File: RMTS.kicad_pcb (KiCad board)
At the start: 2 copper layers, 78.1 x 50.2 mm, 86 parts, among them J1 Screw_Terminal_01x02, J10 CONN_02, J11 CONN_02, J12 CONN_02, J2 Programmer, J3 Screw_Terminal_01x03, J4 Screw_Terminal_01x04, J5 Screw_Terminal_01x02, J6 Screw_Terminal_01x02, J7 Micro_SD_Card_Det_Hirose_DM3AT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

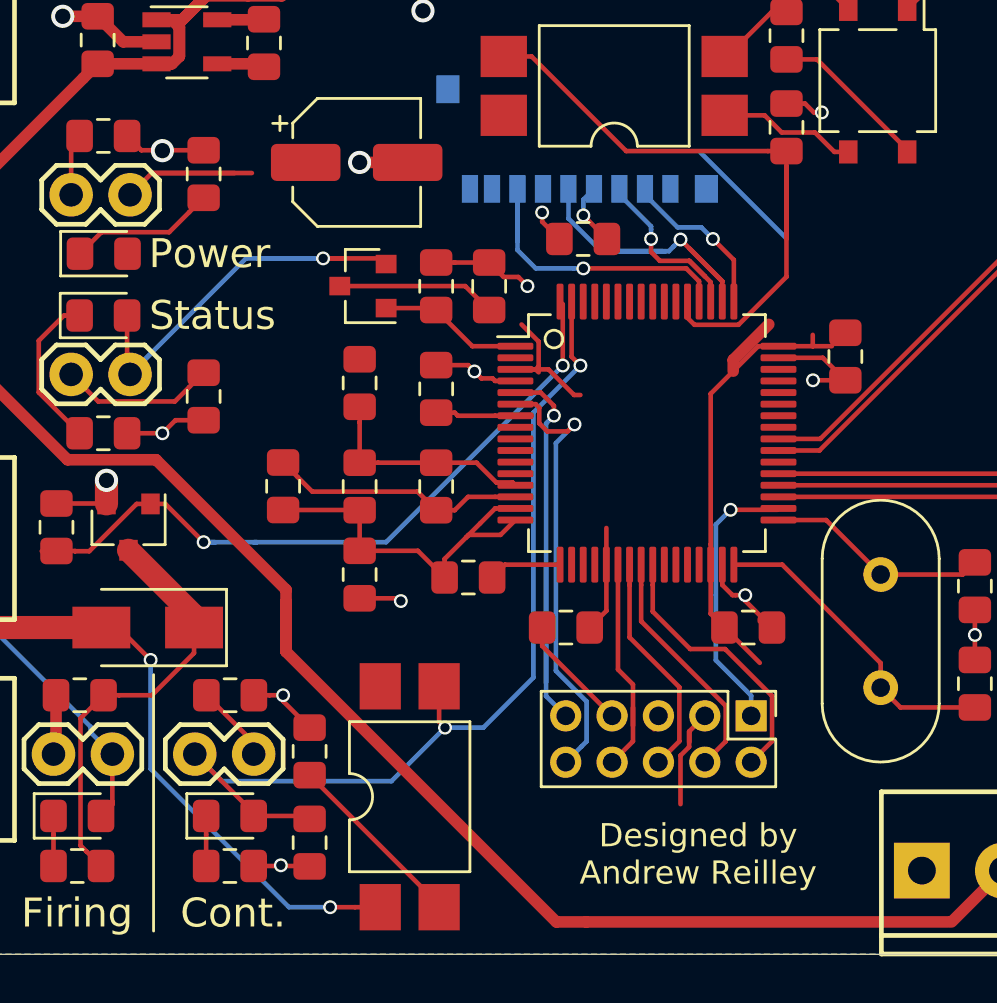
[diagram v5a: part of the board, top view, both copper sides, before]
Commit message: Adjust silkscreen
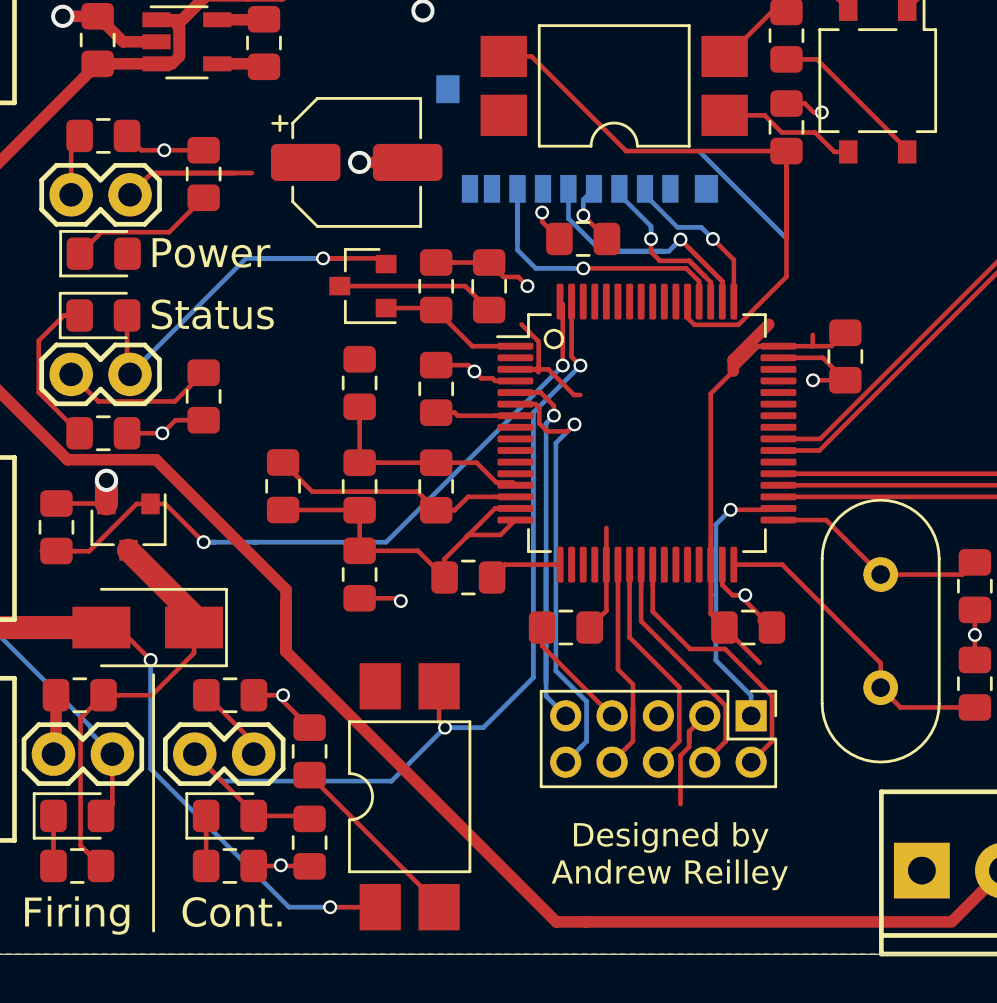
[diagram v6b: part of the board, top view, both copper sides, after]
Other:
- board text added: "Load Cell"
- board text added: "Main"
- board text added: "Pressure"
- board text added: "Pyro"
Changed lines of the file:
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@@
   (general
     (thickness 1.6)
-    (drawings 33)
-    (tracks 656)
+    (drawings 39)
+    (tracks 657)
     (zones 0)
     (modules 86)
@@
       (net 98 "Net-(J10-Pad2)") (solder_mask_margin 0.1016))
   )
+  (gr_text "Load Cell" (at 196.088 111.252) (layer B.SilkS)
+    (effects (font (size 1.25 1.25) (thickness 0.25)) (justify mirror))
+  )
+  (gr_text Pressure (at 182.499 111.252) (layer B.SilkS)
+    (effects (font (size 1.25 1.25) (thickness 0.25)) (justify mirror))
+  )
+  (gr_text Pyro (at 133.858 104.013 -90) (layer B.SilkS)
+    (effects (font (size 1.25 1.25) (thickness 0.25)) (justify mirror))
+  )
+  (gr_text Main (at 134.112 72.0725 -90) (layer B.SilkS)
+    (effects (font (size 1.25 1.25) (thickness 0.25)) (justify mirror))
+  )
+  (gr_text - (at 138.811 73.914 90) (layer B.SilkS)
+    (effects (font (size 1.25 1.25) (thickness 0.25)) (justify mirror))
+  )
+  (gr_text + (at 138.811 70.4215 90) (layer B.SilkS)
+    (effects (font (size 1.25 1.25) (thickness 0.25)) (justify mirror))
+  )
   (gr_line (start 132.08 111.887) (end 132.08 62.738) (layer Edge.Cuts) (width 0.05))
   (gr_line (start 209.677 112.395) (end 132.588 112.395) (layer Edge.Cuts) (width 0.05))
@@
     (effects (font (size 1.25 1.25) (thickness 0.2)))
   )
-  (gr_text "Designed by\nAndrew Reilley" (at 169.418 108.077) (layer F.SilkS)
+  (gr_text "Designed by\nAndrew Reilley" (at 168.2115 108.077) (layer F.SilkS)
     (effects (font (size 1 1) (thickness 0.25)))
   )
@@
     (effects (font (size 1.25 1.25) (thickness 0.25)) (justify mirror))
   )
-  (gr_text + (at 133.985 102.235 90) (layer B.SilkS)
+  (gr_text + (at 138.811 102.235 90) (layer B.SilkS)
     (effects (font (size 1.25 1.25) (thickness 0.25)) (justify mirror))
   )
-  (gr_text - (at 133.985 105.791 90) (layer B.SilkS)
+  (gr_text - (at 138.811 105.791 90) (layer B.SilkS)
     (effects (font (size 1.25 1.25) (thickness 0.25)) (justify mirror))
   )
-  (gr_text S- (at 197.612 110.998) (layer B.SilkS)
+  (gr_text S- (at 197.612 106.426) (layer B.SilkS)
     (effects (font (size 1.25 1.25) (thickness 0.25)) (justify mirror))
   )
-  (gr_text S+ (at 201.168 110.998) (layer B.SilkS)
+  (gr_text S+ (at 201.168 106.426) (layer B.SilkS)
     (effects (font (size 1.25 1.25) (thickness 0.25)) (justify mirror))
   )
-  (gr_text + (at 194.31 110.998) (layer B.SilkS)
+  (gr_text + (at 194.31 106.426) (layer B.SilkS)
     (effects (font (size 1.25 1.25) (thickness 0.25)) (justify mirror))
   )
-  (gr_text - (at 190.754 110.998) (layer B.SilkS)
+  (gr_text - (at 190.754 106.426) (layer B.SilkS)
     (effects (font (size 1.25 1.25) (thickness 0.25)) (justify mirror))
   )
-  (gr_text SIG (at 186.055 111.125) (layer B.SilkS)
+  (gr_text SIG (at 186.055 106.426) (layer B.SilkS)
     (effects (font (size 1.25 1.25) (thickness 0.25)) (justify mirror))
   )
-  (gr_text + (at 182.626 111.125) (layer B.SilkS)
+  (gr_text + (at 182.5625 106.426) (layer B.SilkS)
     (effects (font (size 1.25 1.25) (thickness 0.25)) (justify mirror))
   )
-  (gr_text - (at 179.07 111.125) (layer B.SilkS)
+  (gr_text - (at 179.07 106.426) (layer B.SilkS)
     (effects (font (size 1.25 1.25) (thickness 0.25)) (justify mirror))
   )
@@
   (segment (start 158.115 82.55) (end 158.915 82.55) (width 0.2) (layer F.Cu) (net 1))
   (segment (start 145.397 77.706) (end 144.78 77.089) (width 0.2) (layer F.Cu) (net 1))
-  (segment (start 148.082 77.706) (end 145.397 77.706) (width 0.2) (layer F.Cu) (net 1))
-  (via (at 146.304 77.724) (size 1) (drill 0.66) (layers F.Cu B.Cu) (net 1))
+  (segment (start 148.082 77.706) (end 146.3855 77.706) (width 0.2) (layer F.Cu) (net 1))
   (segment (start 144.78 89.916) (end 146.304 89.916) (width 0.2) (layer F.Cu) (net 1))
   (via (at 146.304 89.916) (size 0.6) (drill 0.4) (layers F.Cu B.Cu) (net 1))
@@
   (segment (start 143.891 92.964) (end 143.891 91.948) (width 1) (layer F.Cu) (net 1))
   (via (at 143.891 91.948) (size 1) (drill 0.66) (layers F.Cu B.Cu) (net 1))
+  (segment (start 146.3855 77.706) (end 145.397 77.706) (width 0.2) (layer F.Cu) (net 1))
+  (via (at 146.3855 77.706) (size 0.6) (drill 0.4) (layers F.Cu B.Cu) (net 1))
   (segment (start 202.565 64.6176) (end 202.565 68.453) (width 0.2) (layer F.Cu) (net 2))
   (segment (start 162.535011 85.959903) (end 161.79848 85.223372) (width 0.2) (layer F.Cu) (net 2))

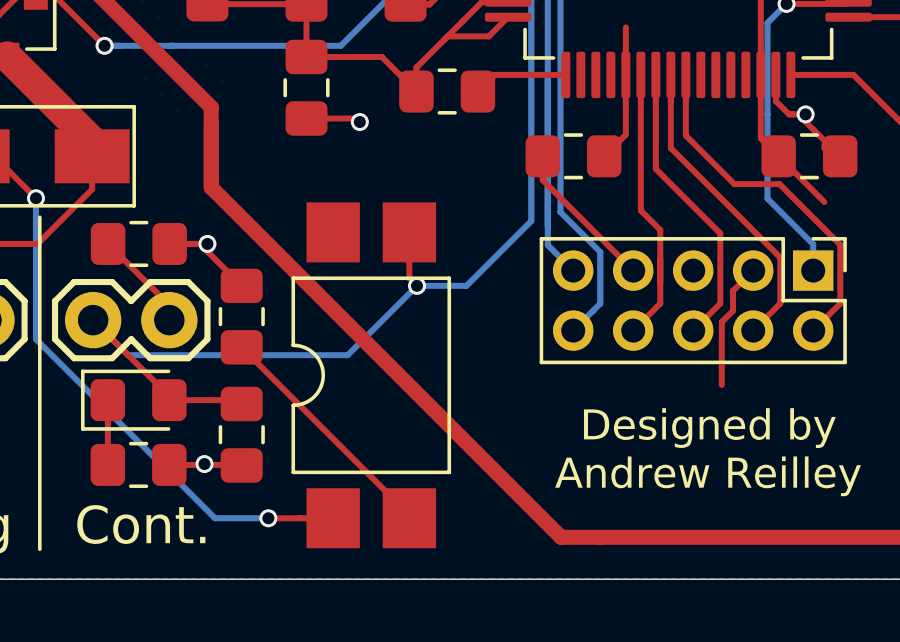
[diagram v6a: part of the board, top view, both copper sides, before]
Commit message: Get 5v from programmer
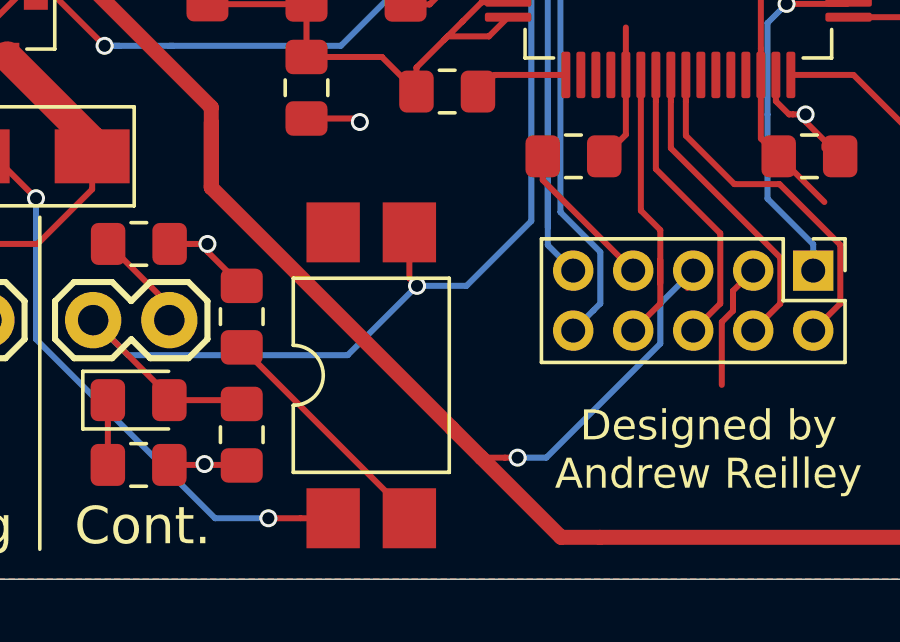
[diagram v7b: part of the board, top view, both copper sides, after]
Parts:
- TP5: value 5V -> LC
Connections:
- J2 pad 5: GND -> +5V
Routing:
- net +5V: track 161.5 -> 172.6 mm, vias 0 -> 1
- net GND: track 85.6 -> 84.9 mm
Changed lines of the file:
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@@
     (thickness 1.6)
     (drawings 39)
-    (tracks 657)
+    (tracks 666)
     (zones 0)
     (modules 86)
@@
       (effects (font (size 1 1) (thickness 0.15)))
     )
-    (fp_text value 5V (at 0 2.05) (layer F.Fab)
+    (fp_text value LC (at 0 2.05) (layer F.Fab)
       (effects (font (size 1 1) (thickness 0.15)))
     )
@@
       (net 12 /PTA1))
     (pad 5 thru_hole oval (at 0 4 270) (size 1.35 1.35) (drill 0.8) (layers *.Cu *.Mask)
-      (net 1 GND))
+      (net 105 +5V))
     (pad 4 thru_hole oval (at 2 2 270) (size 1.35 1.35) (drill 0.8) (layers *.Cu *.Mask)
       (net 11 /PTA2))
@@
   (segment (start 162.687 99.091) (end 162.687 98.298) (width 0.2) (layer F.Cu) (net 1))
   (segment (start 165.704 102.108) (end 162.687 99.091) (width 0.2) (layer F.Cu) (net 1))
-  (segment (start 167.505001 102.020999) (end 167.505001 102.686037) (width 0.2) (layer F.Cu) (net 1))
+  (segment (start 167.505001 102.020999) (end 167.505001 102.686037) (width 0.2) (layer F.Cu) (net 105))
   (segment (start 156.886 78.232) (end 155.286 78.232) (width 0.5) (layer F.Cu) (net 1))
   (via (at 154.813 78.232) (size 1) (drill 0.66) (layers F.Cu B.Cu) (net 1))
@@
   (segment (start 164.592 110.998) (end 180.213 110.998) (width 0.5) (layer F.Cu) (net 105))
   (segment (start 151.638 97.174728) (end 151.638 99.337602) (width 0.5) (layer F.Cu) (net 105))
-  (segment (start 151.638 99.337602) (end 163.298398 110.998) (width 0.5) (layer F.Cu) (net 105))
   (segment (start 163.298398 110.998) (end 164.592 110.998) (width 0.5) (layer F.Cu) (net 105))
   (segment (start 194.426 96.852) (end 194.426 95.602) (width 0.5) (layer F.Cu) (net 105))
@@
   (segment (start 137.541 86.388728) (end 142.211272 91.059) (width 0.5) (layer F.Cu) (net 105))
   (segment (start 137.541 79.9465) (end 137.541 86.388728) (width 0.5) (layer F.Cu) (net 105))
+  (segment (start 151.638 99.337602) (end 159.658949 107.358551) (width 0.5) (layer F.Cu) (net 105))
+  (segment (start 159.658949 107.358551) (end 160.643199 108.342801) (width 0.5) (layer F.Cu) (net 105))
+  (segment (start 160.643199 108.342801) (end 163.298398 110.998) (width 0.5) (layer F.Cu) (net 105))
+  (segment (start 162.804161 108.342801) (end 161.849699 108.342801) (width 0.2) (layer B.Cu) (net 105))
+  (segment (start 166.606001 104.540961) (end 162.804161 108.342801) (width 0.2) (layer B.Cu) (net 105))
+  (segment (start 166.606001 103.205999) (end 166.606001 104.540961) (width 0.2) (layer B.Cu) (net 105))
+  (segment (start 167.704 102.108) (end 166.606001 103.205999) (width 0.2) (layer B.Cu) (net 105))
+  (via (at 161.849699 108.342801) (size 0.6) (drill 0.4) (layers F.Cu B.Cu) (net 105))
+  (segment (start 161.425435 108.342801) (end 160.643199 108.342801) (width 0.2) (layer F.Cu) (net 105))
+  (segment (start 161.849699 108.342801) (end 161.425435 108.342801) (width 0.2) (layer F.Cu) (net 105))
   (segment (start 143.4035 68.006) (end 143.383 68.0265) (width 0.5) (layer F.Cu) (net 106))
   (segment (start 143.383 67.3515) (end 143.6785 67.056) (width 0.5) (layer F.Cu) (net 106))

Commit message: Cleanup
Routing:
- net +3V3: track 78.9 -> 71.4 mm
- net /SD_CLK: track 17.7 -> 12.3 mm
- net Net-(C10-Pad1): track 3.16 -> 4.26 mm
